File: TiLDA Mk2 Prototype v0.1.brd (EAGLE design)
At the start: 68 x 100 mm, 216 parts, among them IC1 ATSAM3X8EA-AU, IC2 MPU-6050, IC3 SRF-V1.2, IC4 LTC4160, IC5 S25FL216K0PMFI011, IC6 AT45DB161E-SSHFHA (NP), IC7 HMC5883LSMD (NP), IC8 MCP1825T-3302E/DC, J1 ZX62-AB-5PA(11), J2 FCI 62684-401100ALF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

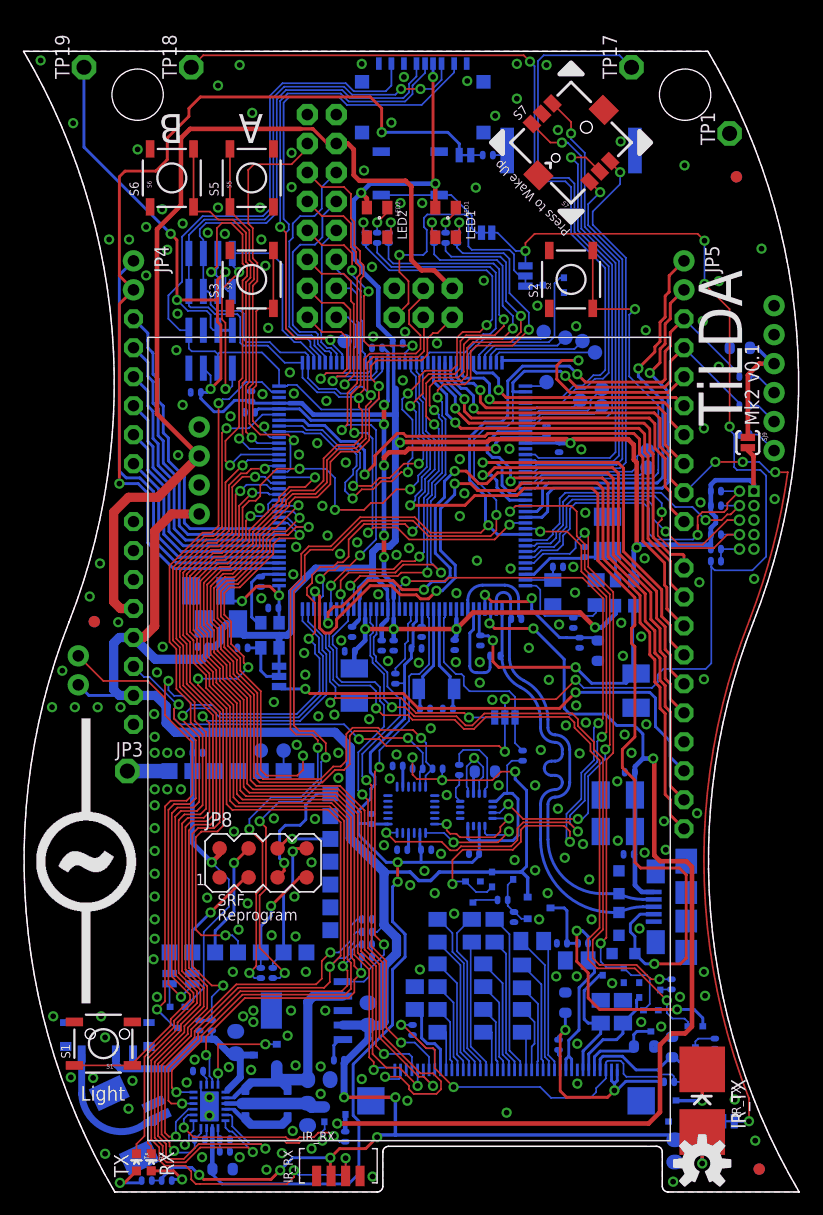
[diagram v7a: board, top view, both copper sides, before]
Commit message: Prototype: Corrected Joystick pins
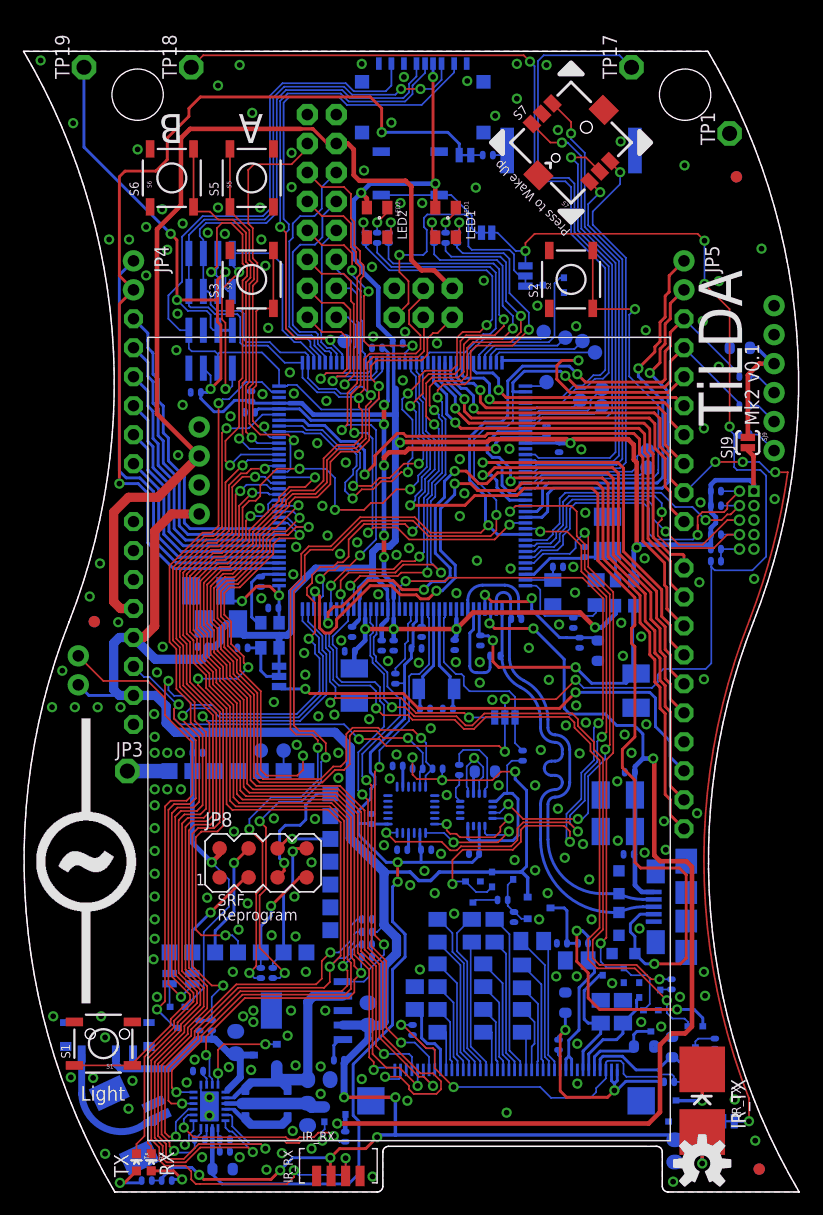
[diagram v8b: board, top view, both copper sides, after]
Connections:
- net BUTTON_LEFT: now also IC1.16, S7.C; no longer IC1.13, S7.B
- net BUTTON_RIGHT: now also IC1.13, S7.B; no longer IC1.16, S7.C
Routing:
- net BUTTON_RIGHT: track 38.1 -> 40.9 mm
- net BUTTON_LEFT: track 40.9 -> 38.1 mm
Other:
- board text added: "SJ9"
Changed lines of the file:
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@@
 <text x="58.2" y="2.6" size="0.6096" layer="22" ratio="15" rot="MR90">C37</text>
 <text x="61" y="73.7" size="0.6096" layer="22" ratio="15" rot="MR0">C38</text>
+<text x="62.15" y="64.3" size="1.016" layer="21" ratio="15" rot="R90">SJ9</text>
 </plain>
 <attributes>
@@
 <wire x1="48" y1="90.7" x2="48.6" y2="90.1" width="0.15" layer="16"/>
 </signal>
-<signal name="BUTTON_LEFT">
+<signal name="BUTTON_RIGHT">
 <contactref element="S7" pad="B"/>
 <contactref element="IC1" pad="13"/>
@@
 <wire x1="19.8" y1="65.15" x2="22.4" y2="65.15" width="0.15" layer="16"/>
 </signal>
-<signal name="BUTTON_RIGHT">
-<contactref element="S7" pad="C"/>
-<contactref element="IC1" pad="16"/>
-<wire x1="44" y1="63.15" x2="44.8" y2="63.15" width="0.15" layer="16"/>
-<wire x1="44.8" y1="63.15" x2="45.1" y2="63.45" width="0.15" layer="16"/>
-<wire x1="45.1" y1="63.45" x2="52.3" y2="63.45" width="0.15" layer="16"/>
-<wire x1="52.3" y1="63.45" x2="52.8" y2="63.95" width="0.15" layer="16"/>
-<wire x1="52.8" y1="63.95" x2="52.8" y2="81.9" width="0.15" layer="16"/>
-<wire x1="52.8" y1="81.9" x2="49.9" y2="84.8" width="0.15" layer="16"/>
-<wire x1="49.9" y1="84.8" x2="49.9" y2="85.95" width="0.15" layer="16"/>
-<wire x1="51.429465625" y1="90.373653125" x2="51.429465625" y2="90.270534375" width="0.15" layer="1"/>
-<wire x1="51.429465625" y1="90.270534375" x2="52.3" y2="89.4" width="0.15" layer="1"/>
-<via x="52.3" y="89.4" extent="1-16" drill="0.5"/>
-<wire x1="52.3" y1="89.4" x2="52.3" y2="88.35" width="0.15" layer="16"/>
-<wire x1="52.3" y1="88.35" x2="49.9" y2="85.95" width="0.15" layer="16"/>
-</signal>
 <signal name="SCREEN_LEFT">
 <contactref element="S2" pad="3"/>
@@
 <wire x1="17.05" y1="9.4" x2="17.05" y2="10.4" width="0.15" layer="16"/>
 <via x="17.05" y="10.4" extent="1-16" drill="0.5"/>
-<wire x1="17.05" y1="10.4" x2="17.05" y2="12.95" width="0.15" layer="1"/>
-<wire x1="17.05" y1="12.95" x2="21.2" y2="12.95" width="0.15" layer="1"/>
+<wire x1="17.05" y1="10.4" x2="17.05" y2="12.45" width="0.15" layer="1"/>
+<wire x1="17.05" y1="12.45" x2="17.55" y2="12.95" width="0.15" layer="1"/>
+<wire x1="17.55" y1="12.95" x2="21.2" y2="12.95" width="0.15" layer="1"/>
 <via x="21.2" y="12.95" extent="1-16" drill="0.5"/>
 <wire x1="21.2" y1="12.95" x2="22.2" y2="12.95" width="0.15" layer="16"/>
@@
 <signal name="3V1">
 </signal>
-<signal name="BUTTON_LEFT1">
+<signal name="BUTTON_LEFT">
+<contactref element="S7" pad="C"/>
+<contactref element="IC1" pad="16"/>
+<wire x1="44" y1="63.15" x2="44.8" y2="63.15" width="0.15" layer="16"/>
+<wire x1="44.8" y1="63.15" x2="45.1" y2="63.45" width="0.15" layer="16"/>
+<wire x1="45.1" y1="63.45" x2="52.3" y2="63.45" width="0.15" layer="16"/>
+<wire x1="52.3" y1="63.45" x2="52.8" y2="63.95" width="0.15" layer="16"/>
+<wire x1="52.8" y1="63.95" x2="52.8" y2="81.9" width="0.15" layer="16"/>
+<wire x1="52.8" y1="81.9" x2="49.9" y2="84.8" width="0.15" layer="16"/>
+<wire x1="49.9" y1="84.8" x2="49.9" y2="85.95" width="0.15" layer="16"/>
+<wire x1="51.429465625" y1="90.373653125" x2="51.429465625" y2="90.270534375" width="0.15" layer="1"/>
+<wire x1="51.429465625" y1="90.270534375" x2="52.3" y2="89.4" width="0.15" layer="1"/>
+<via x="52.3" y="89.4" extent="1-16" drill="0.5"/>
+<wire x1="52.3" y1="89.4" x2="52.3" y2="88.35" width="0.15" layer="16"/>
+<wire x1="52.3" y1="88.35" x2="49.9" y2="85.95" width="0.15" layer="16"/>
 </signal>
 <signal name="BUTTON_UP1">
